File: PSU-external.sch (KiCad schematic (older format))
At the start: 31 parts

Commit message: Simplified external PSU, now that I've decided to put it in its own case.
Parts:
- removed C? (x2): 10u, symbol CP1
- removed C? (x2): 47n, symbol C
- removed D? (x2): BRIDGE_SML, symbol BRIDGE_SML
- removed D? (x2): DIODE, ~, symbol DIODE
- removed D? (x2): ZENER, symbol ZENER
- removed D? (x2): DIODESCH, symbol DIODESCH
- removed R? (x2): 560, symbol R
- removed R? (x2): 7.5k, symbol R
- removed R? (x2): 1k, symbol R
- removed T?: AMGIS_L01, symbol AMGIS_L01
- removed T?: TAMURA_3FD-3XX, symbol TAMURA_3FD-3XX
- removed U?: LM317T, TO-220, symbol LM317T
- removed U? (x2): SCR_SML, symbol SCR_SML
- removed U?: LM337T, TO-220, symbol LM337T
- added C? (x2): C, ~, symbol C
- added C? (x3): 1u, symbol CP1
- added D? (x7): 1N4001, ~, symbol DIODE
- added D? (x4): RL205, ~, symbol DIODE
- added J?: IEC-C13-SOCKET, ~, symbol IEC-C13-SOCKET
- added R? (x2): R, ~, symbol R
- added T?: TRIAD-FS48-750-C2, symbol TRIAD-FS48-750-C2
- added T?: TRIAD-FS16-400-C2, symbol TRIAD-FS16-400-C2
- added U? (x2): SMP50, symbol SMP50
- added U?: LM7918CT, TO-220, symbol LM7918CT
- added U?: LM7818CT, TO-220, symbol LM7818CT
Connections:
- wire segments 61 -> 80
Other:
- note added: "* 100 nF needed?"
- note removed: "BR diodes -- caps? Do I need fast diodes then?\nLT4635 instead of crowbar?\nWhat to do about Pri -> Sec shorts?\nChange reg setting to account for loss across Schottkys"
- note removed: "Change TF. Need something that gives >= 7.6 VRMS out.\nTotal VA >= 3.8 W\nhttp://australia.rs-online.com/web/p/pcb-transformers/0504357/\nhttp://au.mouser.com/ProductDetail/TE-Connectivity-PB/4900-9010RC62/?qs=sGAEpiMZZMvwUzoUXIIvybxvWcHlXqMIJJMreLPLlIY%3d\nhttp://au.mouser.com/ProductDetail/Hammond-Manufacturing/160G10/?qs=sGAEpiMZZMvwUzoUXIIvyW8HfC4QLhUeoMmGdCqPnA8%3d"
- note removed: "TF needs to give >= 17 VRMS out of each secondary.\nTotal VA >= 17 W\nhttp://australia.rs-online.com/web/p/pcb-transformers/1739298/\nhttp://australia.rs-online.com/web/p/pcb-transformers/1739361/\nhttp://au.mouser.com/ProductDetail/Triad-Magnetics/FS36-1000/?qs=sGAEpiMZZMvwUzoUXIIvydH8%2fj5UF54ye%252bQIrzt8fZs%3d\nhttp://au.mouser.com/ProductDetail/Triad-Magnetics/FS48-750/?qs=sGAEpiMZZMvwUzoUXI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"
- moved on the sheet: C?, U?

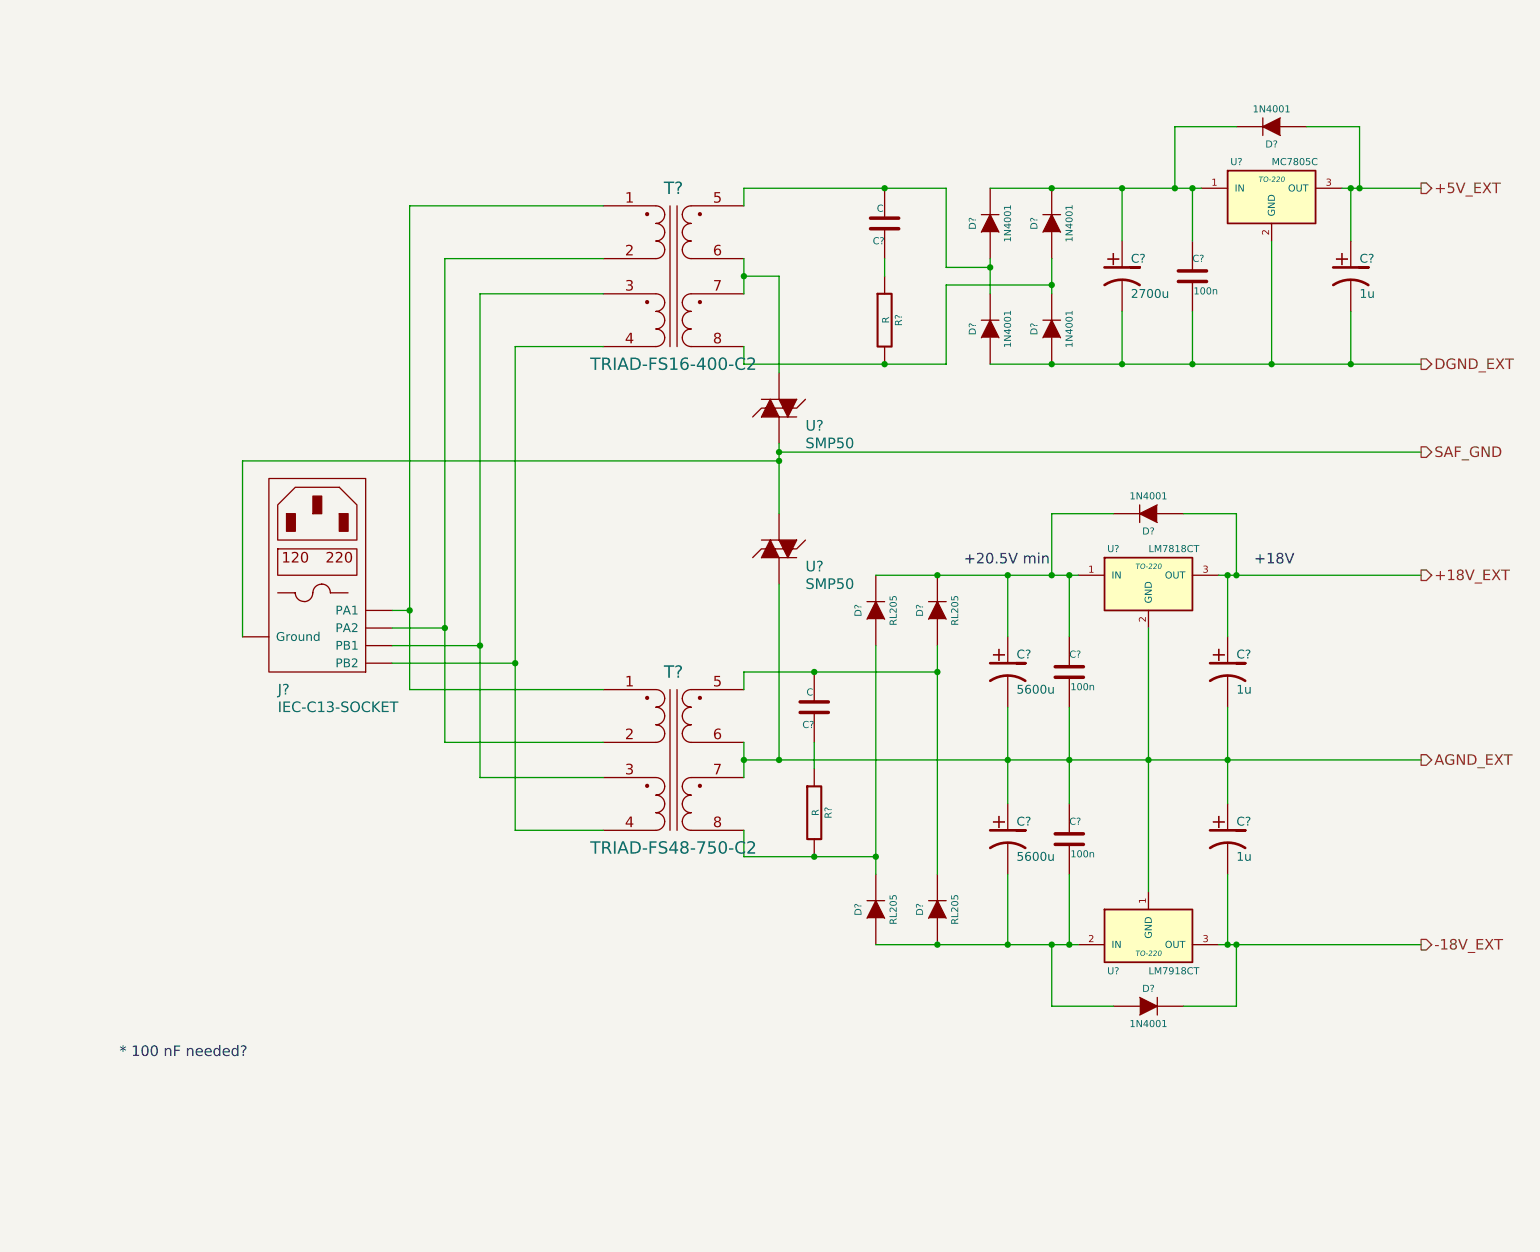
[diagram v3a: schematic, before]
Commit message: Further PSU tweaking for extra safety, added a TODO list.
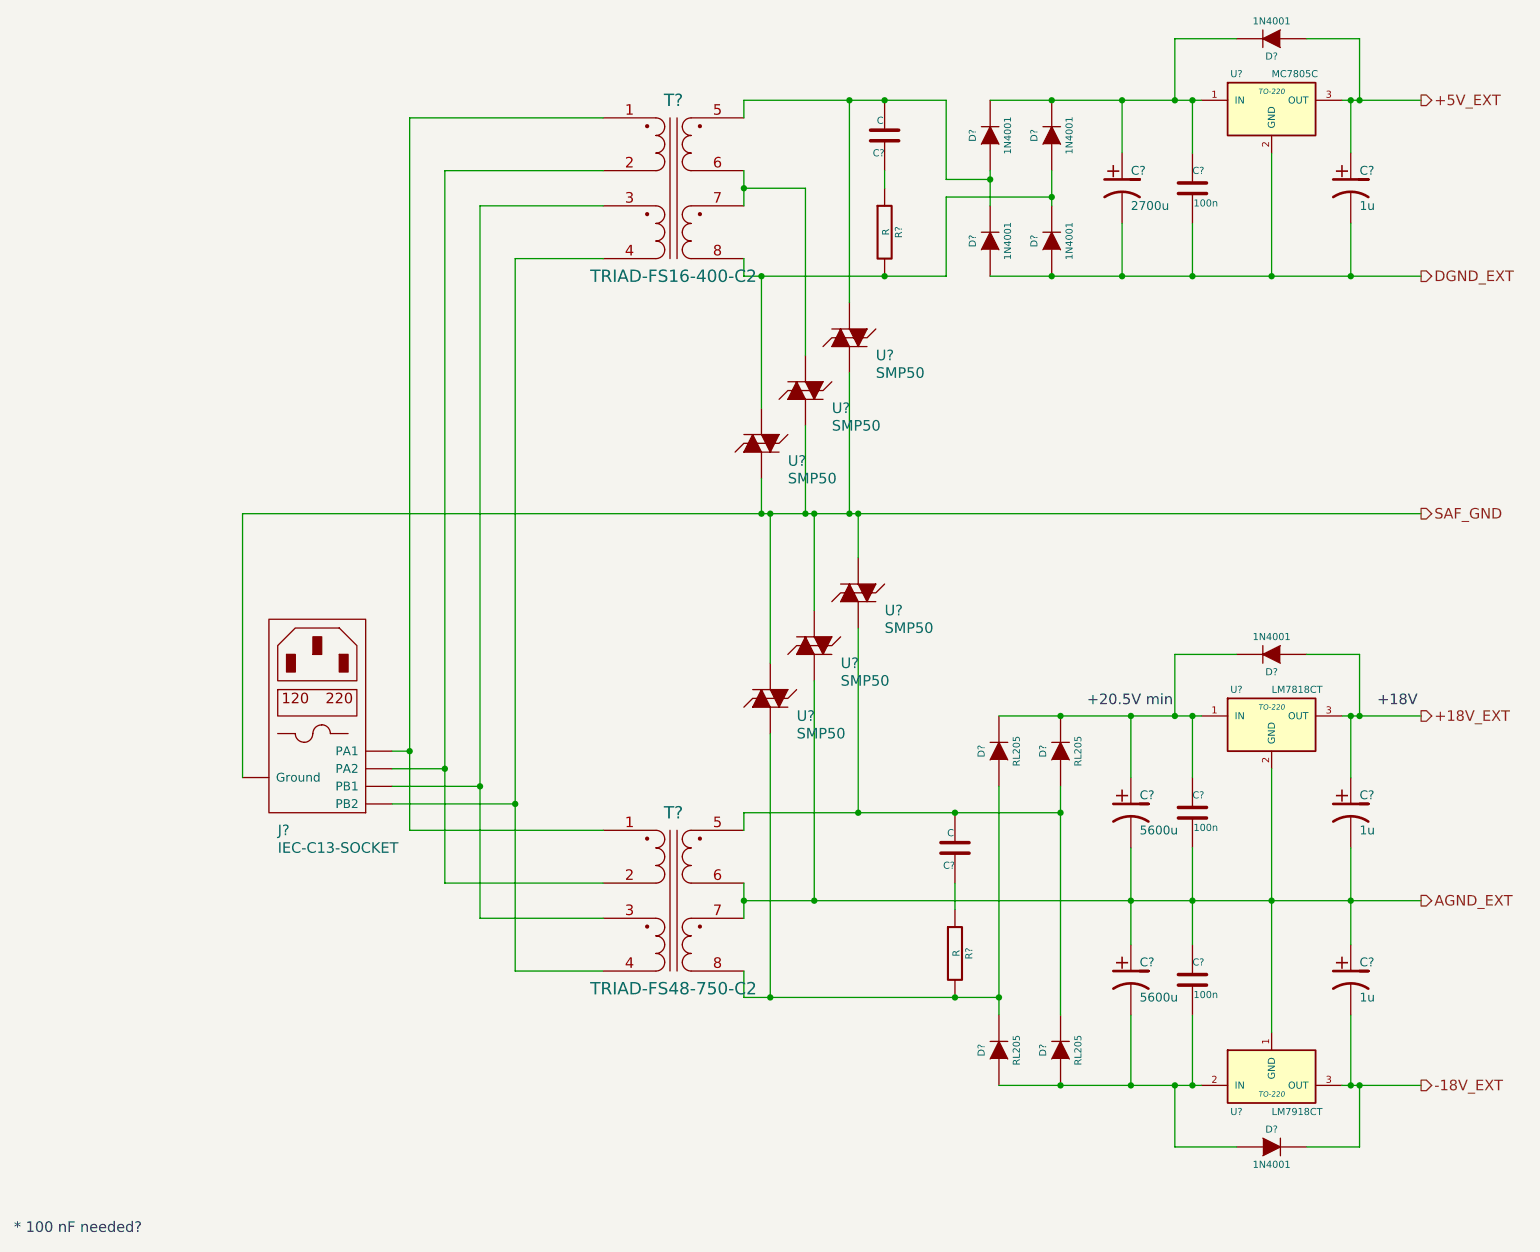
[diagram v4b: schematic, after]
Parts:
- removed U?: SMP50, symbol SMP50
- added U? (x5): SMP50, symbol SMP50
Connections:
- net AGND_EXT: now also U?.~
- net SAF_GND: now also U?.~, U?.~, U?.~, U?.~, U?.~
- net at D?.1 (A), D?.2 (K), R?.2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: now also U?.~ (x2)
- net at C?.2, D?.1 (A), D?.2 (K)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: now also U?.~ (x2)
- net at T?.6 (SB), T?.7 (SC): now also U?.~; no longer U?.~
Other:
- moved on the sheet: C?, D?, J?, R?, T?, U?

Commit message: Many additions; the system's almost together.  Just need to tidy up a few things around the PSU and the input stage.
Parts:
- removed U? (x4): SMP50, symbol SMP50
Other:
- note removed: "* 100 nF needed?"
- moved on the sheet: C?, D?, J?, R?, T?, U?
